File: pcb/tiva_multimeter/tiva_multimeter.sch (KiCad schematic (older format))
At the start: 8 parts

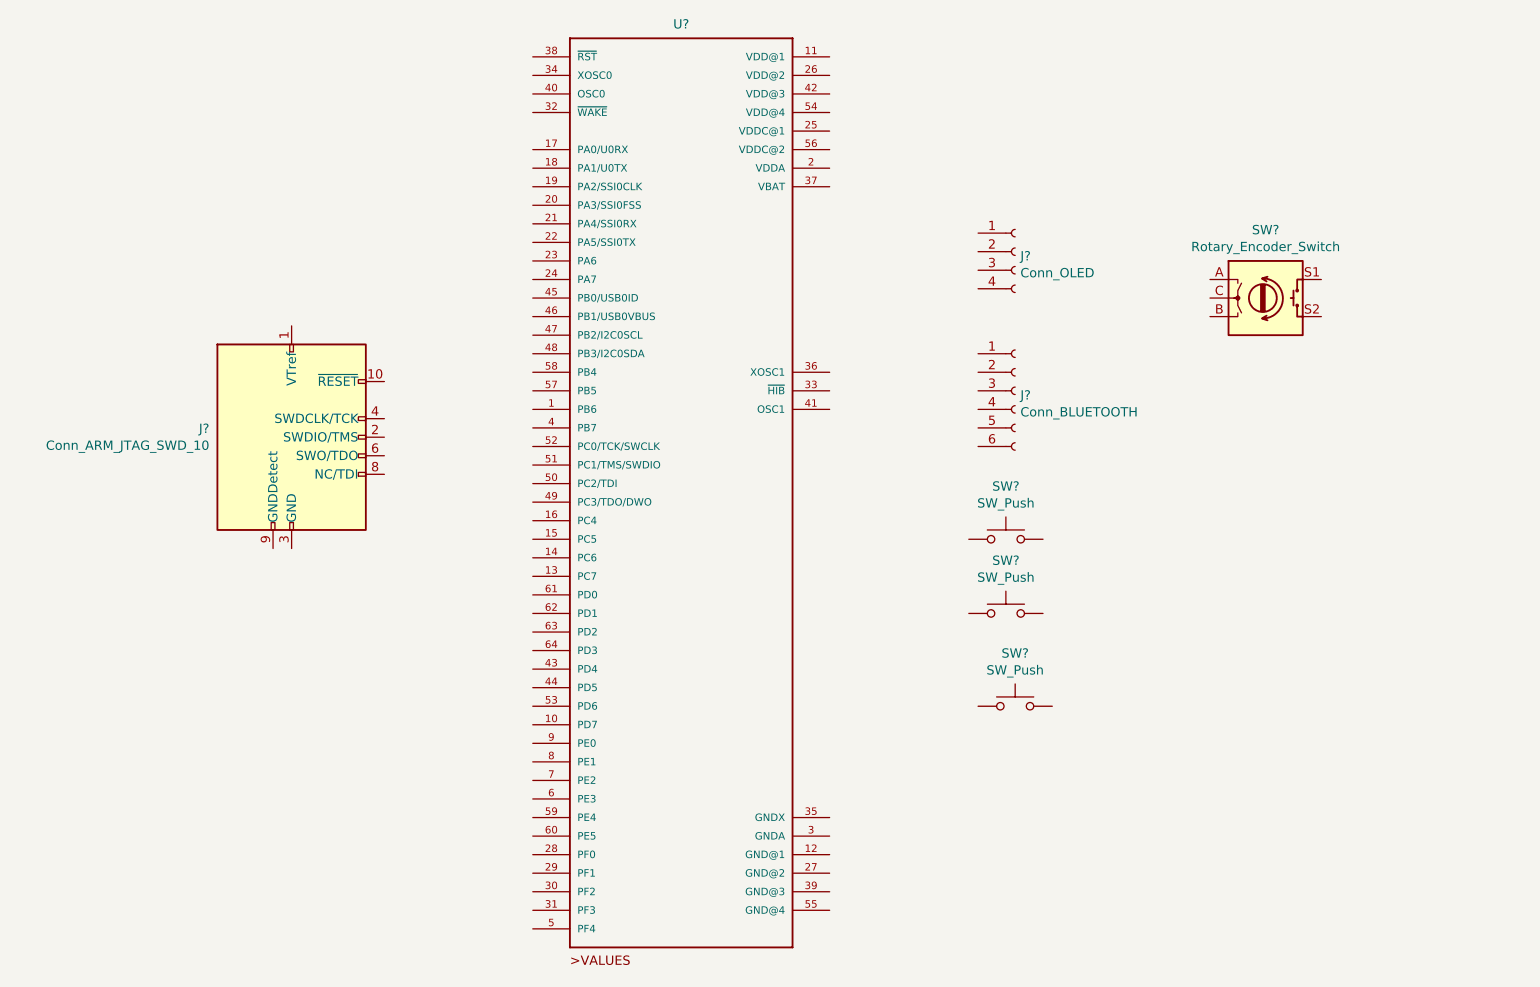
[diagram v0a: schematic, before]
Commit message: fixed gitignore
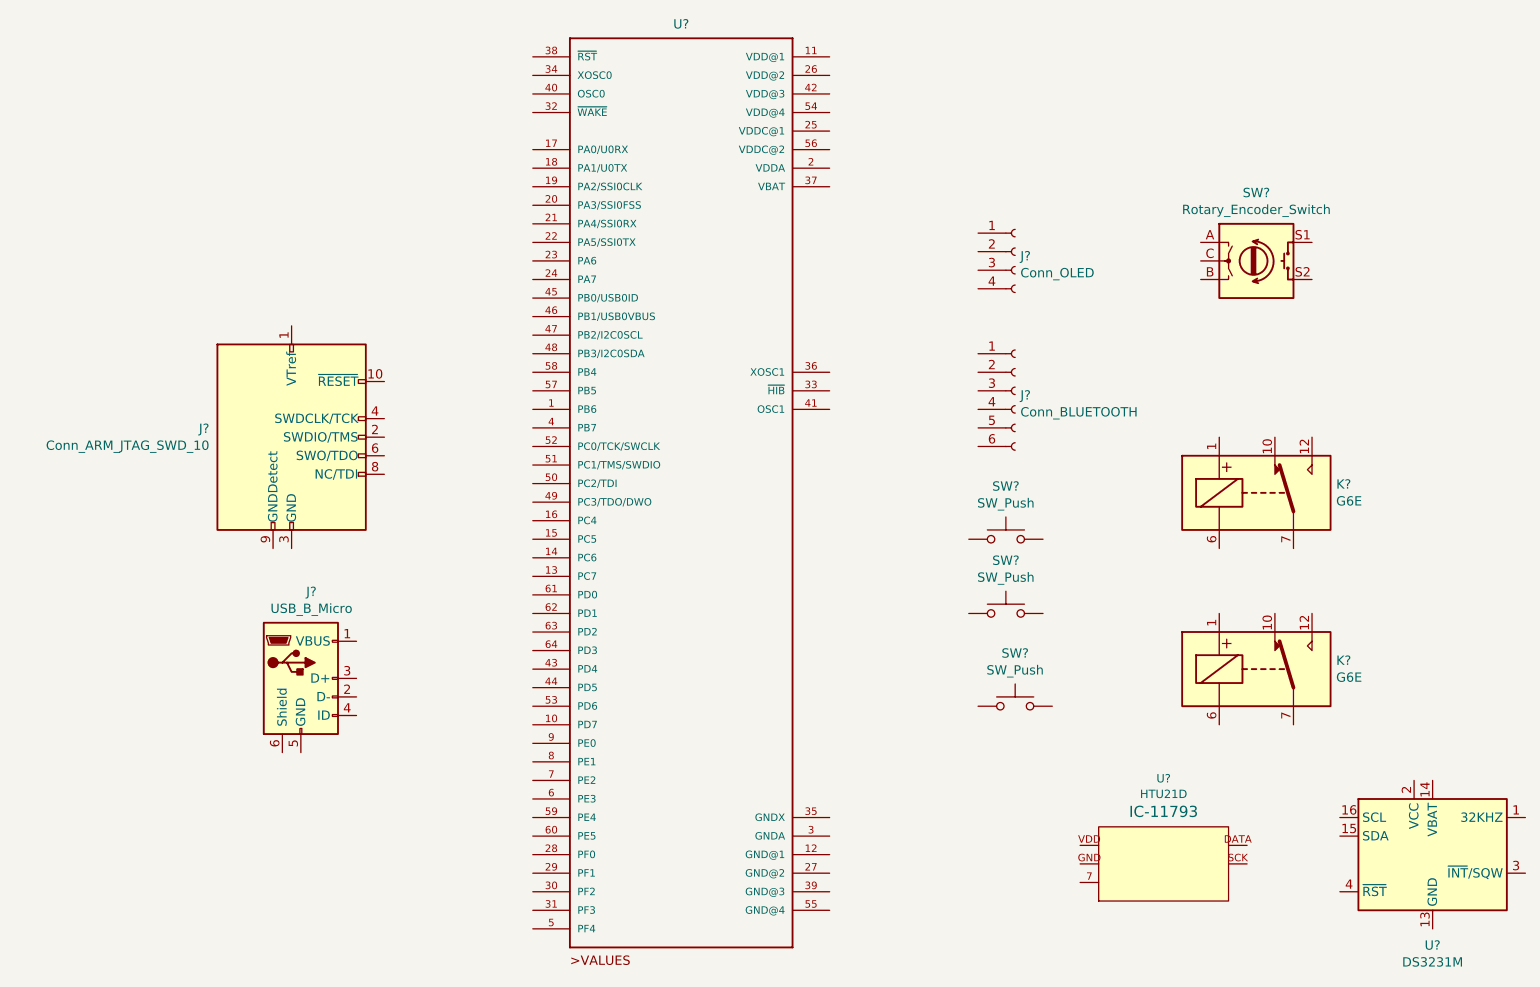
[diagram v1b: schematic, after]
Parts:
- added J?: USB_B_Micro, symbol Connector:USB_B_Micro
- added K? (x2): G6E, Relay_THT:Relay_SPDT_Omron_G6E, symbol Relay:G6E
- added U?: HTU21D, DFN-6-3X3-HTU21D, symbol SparkFun-Sensors:HTU21D
- added U?: DS3231M, Package_SO:SOIC-16W_7.5x10.3mm_P1.27mm, symbol Timer_RTC:DS3231M
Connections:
- new net: U?.10 (GND), U?.11 (GND), U?.12 (GND), U?.13 (GND), U?.5 (GND), U?.6 (GND), U?.7 (GND), U?.8 (GND), U?.9 (GND)
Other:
- moved on the sheet: SW?
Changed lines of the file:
@@
 L Device:Rotary_Encoder_Switch SW?
 U 1 1 5E2C4472
-P 7750 2350
-F 0 "SW?" H 7750 2717 50  0000 C CNN
-F 1 "Rotary_Encoder_Switch" H 7750 2626 50  0000 C CNN
-F 2 "" H 7600 2510 50  0001 C CNN
-F 3 "~" H 7750 2610 50  0001 C CNN
-	1    7750 2350
+P 7700 2150
+F 0 "SW?" H 7700 2517 50  0000 C CNN
+F 1 "Rotary_Encoder_Switch" H 7700 2426 50  0000 C CNN
+F 2 "" H 7550 2310 50  0001 C CNN
+F 3 "~" H 7700 2410 50  0001 C CNN
+	1    7700 2150
 	1    0    0    -1
 $EndComp
@@
 	1    0    0    -1
 $EndComp
+$Comp
+L Relay:G6E K?
+U 1 1 5E2CF753
+P 7700 3400
+F 0 "K?" H 8130 3446 50  0000 L CNN
+F 1 "G6E" H 8130 3355 50  0000 L CNN
+F 2 "Relay_THT:Relay_SPDT_Omron_G6E" H 8830 3370 50  0001 C CNN
+F 3 "https://www.omron.com/ecb/products/pdf/en-g6e.pdf" H 7700 3400 50  0001 C CNN
+	1    7700 3400
+	1    0    0    -1
+$EndComp
+$Comp
+L Relay:G6E K?
+U 1 1 5E2D2425
+P 7700 4350
+F 0 "K?" H 8130 4396 50  0000 L CNN
+F 1 "G6E" H 8130 4305 50  0000 L CNN
+F 2 "Relay_THT:Relay_SPDT_Omron_G6E" H 8830 4320 50  0001 C CNN
+F 3 "https://www.omron.com/ecb/products/pdf/en-g6e.pdf" H 7700 4350 50  0001 C CNN
+	1    7700 4350
+	1    0    0    -1
+$EndComp
+$Comp
+L SparkFun-Sensors:HTU21D U?
+U 1 1 5E2D3C18
+P 7150 5400
+F 0 "U?" H 7200 5860 45  0000 C CNN
+F 1 "HTU21D" H 7200 5776 45  0000 C CNN
+F 2 "DFN-6-3X3-HTU21D" H 7150 5750 20  0001 C CNN
+F 3 "" H 7150 5400 60  0001 C CNN
+F 4 "IC-11793" H 7200 5681 60  0000 C CNN "Field4"
+	1    7150 5400
+	1    0    0    -1
+$EndComp
+$Comp
+L Timer_RTC:DS3231M U?
+U 1 1 5E2DB37E
+P 8650 5350
+F 0 "U?" H 8650 4861 50  0000 C CNN
+F 1 "DS3231M" H 8650 4770 50  0000 C CNN
+F 2 "Package_SO:SOIC-16W_7.5x10.3mm_P1.27mm" H 8650 4750 50  0001 C CNN
+F 3 "http://datasheets.maximintegrated.com/en/ds/DS3231.pdf" H 8920 5400 50  0001 C CNN
+	1    8650 5350
+	1    0    0    -1
+$EndComp
+$Comp
+L Connector:USB_B_Micro J?
+U 1 1 5E2E68E7
+P 2550 4400
+F 0 "J?" H 2607 4867 50  0000 C CNN
+F 1 "USB_B_Micro" H 2607 4776 50  0000 C CNN
+F 2 "" H 2700 4350 50  0001 C CNN
+F 3 "~" H 2700 4350 50  0001 C CNN
+	1    2550 4400
+	1    0    0    -1
+$EndComp

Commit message: added tiva docs
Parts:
- removed K?: G6E, Relay_THT:Relay_SPDT_Omron_G6E, symbol Relay:G6E
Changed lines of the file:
@@
-$Comp
-L Relay:G6E K?
-U 1 1 5E2CF753
-P 7700 3400
-F 0 "K?" H 8130 3446 50  0000 L CNN
-F 1 "G6E" H 8130 3355 50  0000 L CNN
-F 2 "Relay_THT:Relay_SPDT_Omron_G6E" H 8830 3370 50  0001 C CNN
-F 3 "https://www.omron.com/ecb/products/pdf/en-g6e.pdf" H 7700 3400 50  0001 C CNN
-	1    7700 3400
-	1    0    0    -1
-$EndComp
 $Comp
 L Relay:G6E K?
